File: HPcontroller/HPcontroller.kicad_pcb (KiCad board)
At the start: 2 copper layers, 100 x 62 mm, 45 parts, among them J1 Screw_Terminal_01x02, Q1 Q_Dual_NMOS_S1G1S2G2D2D2D1D1, U1 Adafruit_QTPY_ESP32-C3, U2 NCP81071B, U3 MIC841N, U4 VR10S3V3, U5 ER-OLED0.49-1_MODULE, U6 Adafruit_MAX31850

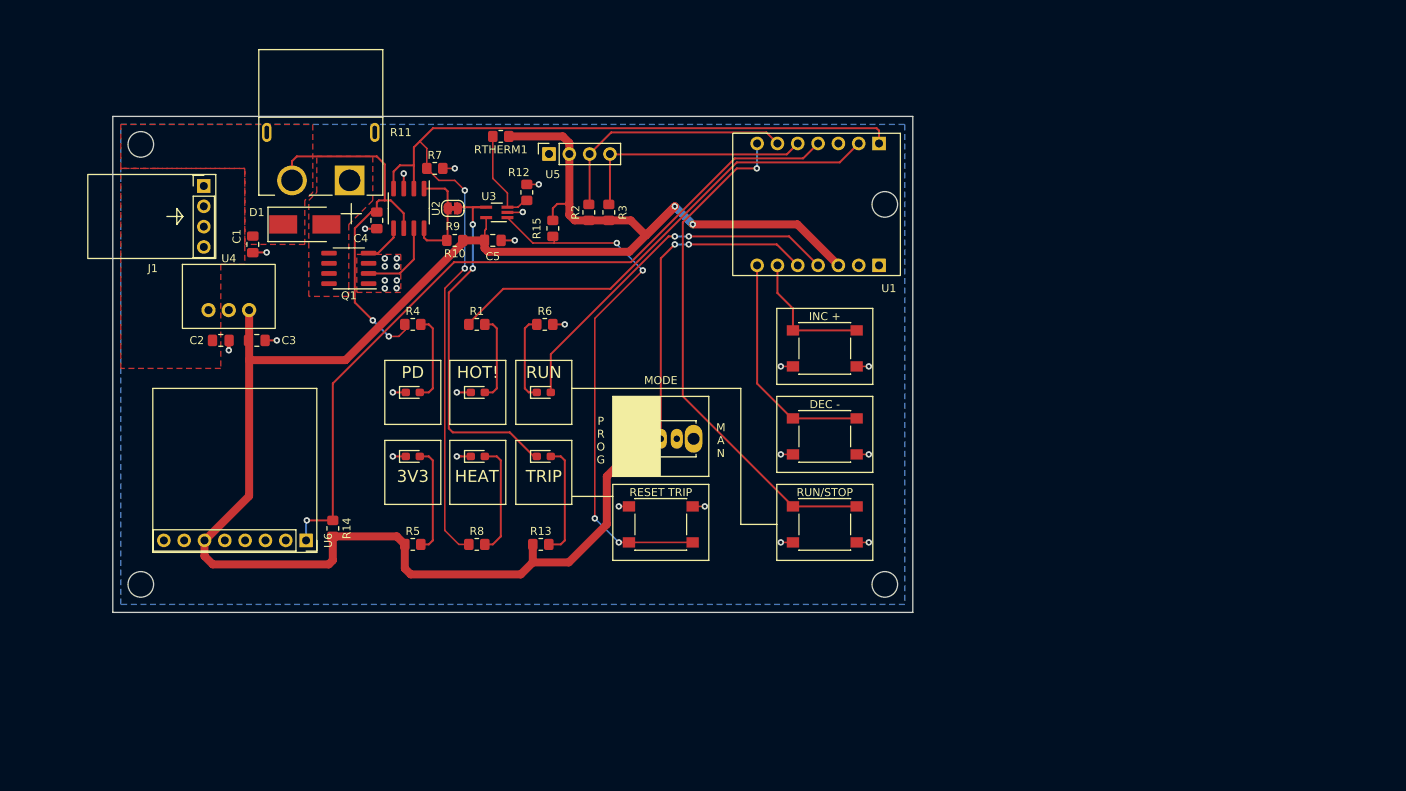
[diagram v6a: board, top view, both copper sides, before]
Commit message: started routing, finished footprintns
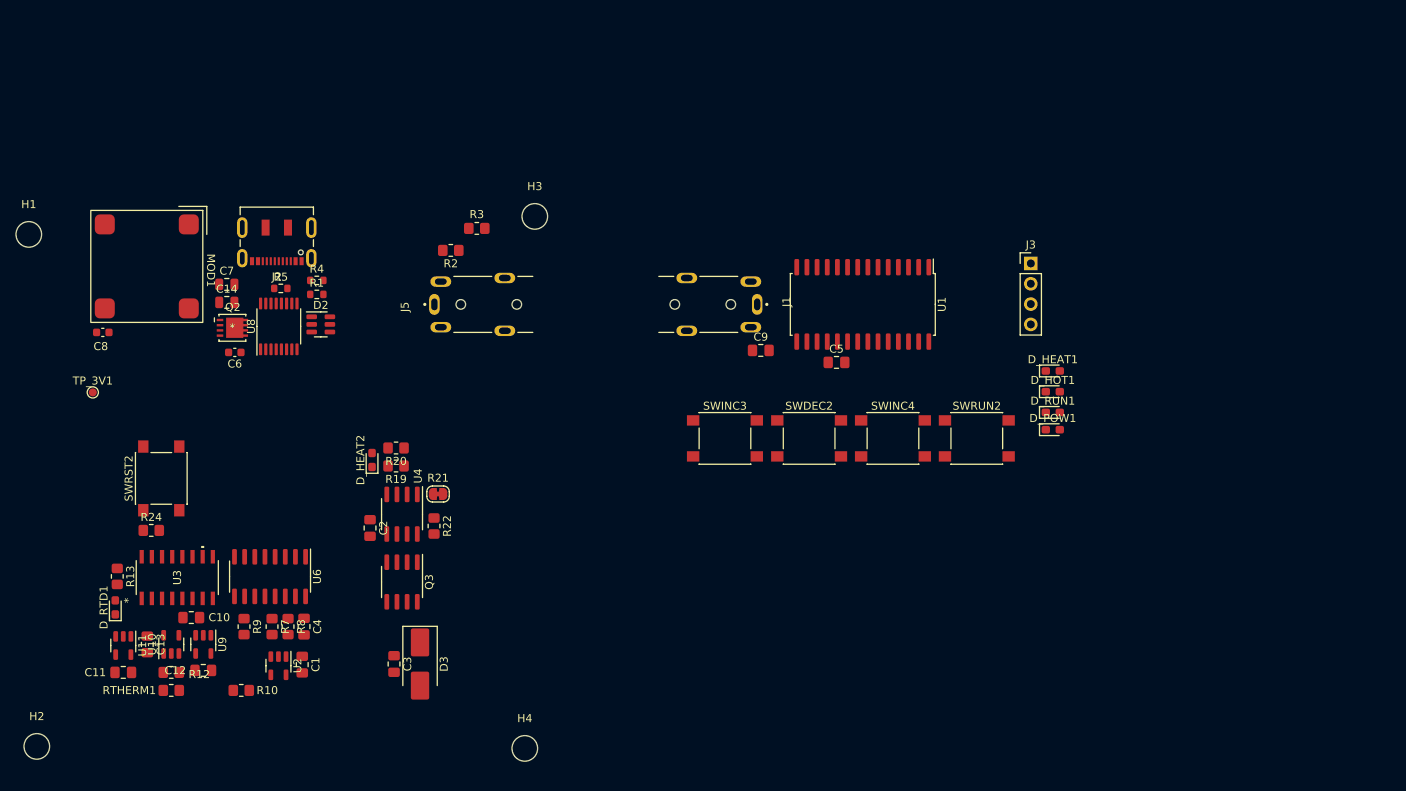
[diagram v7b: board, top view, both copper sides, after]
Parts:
- removed D1: D, Diode_SMD:D_SMB_Handsoldering
- removed D_3V3_POW1, D_PD_POW1: LED, LED_SMD:LED_0603_1608Metric_Pad1.05x0.95mm_HandSolder
- removed Q1: Q_Dual_NMOS_S1G1S2G2D2D2D1D1, Package_SO:SOIC-8_3.9x4.9mm_P1.27mm
- removed R11: R, connector_custom:AMASS_XT60PW-M
- removed R14: 4k7, Resistor_SMD:R_0805_2012Metric_Pad1.20x1.40mm_HandSolder
- removed R15: 10k, Resistor_SMD:R_0805_2012Metric_Pad1.20x1.40mm_HandSolder
- removed R6: 100, Resistor_SMD:R_0805_2012Metric_Pad1.20x1.40mm_HandSolder
- removed SWDEC1, SWINC1, SWRST1, SWRUN1: SW_SPST, Button_Switch_SMD:SW_SPST_PTS645
- removed SWMODE1: SW_SPDT, Button_Switch_THT:SW_Slide_1P2T_CK_OS102011MS2Q
- removed U5: ER-OLED0.49-1_MODULE, Connector_PinSocket_2.54mm:PinSocket_1x04_P2.54mm_Vertical
- added C10: 1uF, Capacitor_SMD:C_0805_2012Metric_Pad1.18x1.45mm_HandSolder, F.Cu at (82.8, 112.1)
- added C11: 1uF, Capacitor_SMD:C_0805_2012Metric_Pad1.18x1.45mm_HandSolder, F.Cu at (74.3, 119.0)
- added C12: 1uF, Capacitor_SMD:C_0805_2012Metric_Pad1.18x1.45mm_HandSolder, F.Cu at (84.3, 118.8)
- added C13: 1uF, Capacitor_SMD:C_0805_2012Metric_Pad1.18x1.45mm_HandSolder, F.Cu at (77.3, 115.5)
- added C14: 10uF, Capacitor_SMD:C_0805_2012Metric, F.Cu at (87.2, 72.8)
- added C6: 1uF, Capacitor_SMD:C_0603_1608Metric, F.Cu at (88.2, 79.0)
- added C7: 10uF, Capacitor_SMD:C_0805_2012Metric, F.Cu at (87.2, 70.5)
- added C8: 22uF, Capacitor_SMD:C_0603_1608Metric, F.Cu at (71.8, 76.5)
- added C9: 1uF, Capacitor_SMD:C_0805_2012Metric_Pad1.18x1.45mm_HandSolder, F.Cu at (154.0, 78.8)
- added D2: ESDA6V1BC6, Package_TO_SOT_SMD:SOT-23-6, F.Cu at (99.0, 75.5)
- added D3: D, Diode_SMD:D_SMB_Handsoldering, F.Cu at (111.4, 118.0)
- added D_HEAT2: LED, LED_SMD:LED_0603_1608Metric_Pad1.05x0.95mm_HandSolder, F.Cu at (105.4, 92.5)
- added D_POW1: LED, LED_SMD:LED_0603_1608Metric_Pad1.05x0.95mm_HandSolder, F.Cu at (190.5, 88.7)
- added J2: USB_C_Receptacle, Connector_USB:USB_C_Receptacle_JAE_DX07S016JA1R1500, F.Cu at (93.5, 64.5)
- added J3: Conn_01x04_Pin, Connector_PinHeader_2.54mm:PinHeader_1x04_P2.54mm_Vertical, F.Cu at (187.8, 67.9)
- added J5: 54-00174, HPfootprint:TENSILITY_54-00174, F.Cu at (120.0, 73.0)
- added MOD1: K7803JT-500R3-LB, HPfootprint:MORNSUN_K7803JT-500R3-LB, F.Cu at (77.2, 68.2)
- added Q2: AON7410, HPfootprint:DFN3X3A_8L_EPA1_P_AOS, F.Cu at (88.0, 75.9)
- added Q3: Q_Dual_NMOS_S1G1S2G2D2D2D1D1, Package_SO:SOIC-8_3.9x4.9mm_P1.27mm, F.Cu at (109.2, 107.7)
- added R19: 10k, Resistor_SMD:R_0805_2012Metric_Pad1.20x1.40mm_HandSolder, F.Cu at (108.4, 93.2)
- added R20: 100, Resistor_SMD:R_0805_2012Metric_Pad1.20x1.40mm_HandSolder, F.Cu at (108.4, 91.0)
- added R21: 0, Jumper:SolderJumper-2_P1.3mm_Bridged_RoundedPad1.0x1.5mm, F.Cu at (113.7, 96.7)
- added R22: 10k, Resistor_SMD:R_0805_2012Metric_Pad1.20x1.40mm_HandSolder, F.Cu at (113.2, 100.7)
- added R24: 10k, Resistor_SMD:R_0805_2012Metric_Pad1.20x1.40mm_HandSolder, F.Cu at (77.8, 101.2)
- added SWDEC2: SW_SPST, Button_Switch_SMD:SW_SPST_PTS645, F.Cu at (160.0, 89.8)
- added SWINC3: SW_SPST, Button_Switch_SMD:SW_SPST_PTS645, F.Cu at (149.5, 89.8)
- added SWINC4: SW_SPST, Button_Switch_SMD:SW_SPST_PTS645, F.Cu at (170.5, 89.8)
- added SWRST2: SW_SPST, Button_Switch_SMD:SW_SPST_PTS645, F.Cu at (79.1, 94.8)
- added SWRUN2: SW_SPST, Button_Switch_SMD:SW_SPST_PTS645, F.Cu at (181.0, 89.8)
- added TP_3V1: TestPoint, TestPoint:TestPoint_Pad_D1.0mm, F.Cu at (70.5, 84.0)
- added U10: SN74LVC1G14DBV, Package_TO_SOT_SMD:SOT-23-5, F.Cu at (80.3, 115.5)
- added U11: SN74LVC1G14DBV, Package_TO_SOT_SMD:SOT-23-5, F.Cu at (74.3, 115.6)
- added U8: IP2721, Package_SO:TSSOP-16_4.4x5mm_P0.65mm, F.Cu at (93.8, 75.8)
- added U9: SN74AHC1G08DBVR, Package_TO_SOT_SMD:SOT-23-5, F.Cu at (84.3, 115.5)
- C1: value 10u -> 1uF
- C2, C4, C5: value C -> 1uF
- C3: value C -> 10u
- J1: value Screw_Terminal_01x02 -> 54-00174; footprint connector_custom:PD_trigger -> HPfootprint:TENSILITY_54-00174
- R1: value 100 -> 5.1k; footprint Resistor_SMD:R_0805_2012Metric_Pad1.20x1.40mm_HandSolder -> Resistor_SMD:R_0603_1608Metric
- R10: value 10k -> RTHERM
- R4: value 1k5 -> 5.1k; footprint Resistor_SMD:R_0805_2012Metric_Pad1.20x1.40mm_HandSolder -> Resistor_SMD:R_0603_1608Metric
- R5: value 100 -> 100k; footprint Resistor_SMD:R_0805_2012Metric_Pad1.20x1.40mm_HandSolder -> Resistor_SMD:R_0603_1608Metric
- R7: value 10k -> 100k
- R8: value 100 -> 10k
- R9: value 0 -> 1k; footprint Jumper:SolderJumper-2_P1.3mm_Bridged_RoundedPad1.0x1.5mm -> Resistor_SMD:R_0805_2012Metric_Pad1.20x1.40mm_HandSolder
- U1: value Adafruit_QTPY_ESP32-C3 -> MCP23017_SO; footprint DevBoards:QTPY ESP32 C3 -> Package_SO:SOIC-28W_7.5x17.9mm_P1.27mm
- U2: value NCP81071B -> MCP3021A1T-E/OT; footprint Package_SO:SOIC-8_3.9x4.9mm_P1.27mm -> Package_TO_SOT_SMD:SOT-23-5
- U3: value MIC841N -> HEF4043BT; footprint Package_TO_SOT_SMD:SOT-353_SC-70-5_Handsoldering -> HPfootprint:SOT109-1_NXP
- U4: value VR10S3V3 -> NCP81071B; footprint DevBoards:3pinDCDC -> Package_SO:SOIC-8_3.9x4.9mm_P1.27mm
- U6: value Adafruit_MAX31850 -> SN74LV4052ADR; footprint Connector_PinSocket_2.54mm:PinSocket_1x08_P2.54mm_Vertical -> Package_SO:SOIC-16_3.9x9.9mm_P1.27mm
- moved H4 81.5 mm to (124.5, 128.5)
- moved RTHERM1 80.6 mm to (80.3, 121.2)
- moved H2 76.4 mm to (63.5, 128.2)
- moved R12 74.7 mm to (80.3, 119.0), turned to 0 degrees
- moved D_HEAT1 72.7 mm to (190.5, 81.3)
- moved D_HOT1 71.9 mm to (190.5, 83.9)
- moved D_RUN1 63.7 mm to (190.5, 86.5)
- moved H3 63.5 mm to (125.8, 62.0)
- moved J1 63.3 mm to (146.8, 73.0), turned to -90 degrees
- moved R10 62.3 mm to (89.1, 121.2), turned to 0 degrees
- moved R7 60.8 mm to (92.9, 113.3), turned to -90 degrees
- moved U3 60.7 mm to (81.1, 107.1), turned to 90 degrees
- moved U2 59.4 mm to (93.7, 118.2)
- moved R9 58.4 mm to (89.4, 113.3), turned to -90 degrees
- moved D_RTD1 56.8 mm to (73.3, 110.9), turned to 90 degrees
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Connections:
- C1 pad 1: VCC -> +3.3V
- C3 pad 1: +3V3 -> VCC
- C4 pad 1: VCC -> +3.3V
- D_HEAT1 pad 2: Net-(D_HEAT1-Pad2) -> /Controlpad/HEAT
- D_HOT1 pad 2: Net-(D_HOT1-Pad2) -> /Controlpad/HOT
- D_RTD1 pad 1: /ThermalProtector/THM_PROT_OUT -> /HEATER DRIVE/ENABLE_HEATER_DRIVE
- D_RUN1 pad 1: Net-(D_RUN1-Pad1) -> GND
- D_RUN1 pad 2: Net-(D_RUN1-Pad2) -> /Controlpad/RUN
- J1 pad 1: VCC -> GND
- J1 pad 2: GND -> /Controlpad/SDA
- R1 pad 1: Net-(R1-Pad1) -> /USB POWER IN/CC1
- R1 pad 2: Net-(D_HOT1-Pad2) -> GND
- R10 pad 1: +3V3 -> +3.3V
- R10 pad 2: Net-(R10-Pad2) -> Net-(U2-Ain)
- R12 pad 1: Net-(R12-Pad1) -> Net-(U3-1S)
- R4 pad 1: VCC -> /USB POWER IN/CC2
- R4 pad 2: Net-(D_PD_POW1-Pad2) -> GND
- R5 pad 1: +3V3 -> VBUS
- R7 pad 1: /FET_DRIVE -> Net-(U6-1Y1)
- R8 pad 1: /FET_DRIVE -> Net-(U6-1Y2)
- R8 pad 2: Net-(D_HEAT1-Pad2) -> GND
- R9 pad 1: /ThermalProtector/THM_PROT_OUT -> Net-(U6-1Y3)
- R9 pad 2: Net-(R10-Pad2) -> GND
- RTHERM1 pad 2: Net-(R12-Pad1) -> Net-(U3-1S)
- U1 pad 1: /FET_DRIVE -> /Controlpad/HEAT
- U1 pad 10: /MODE -> GND
- U1 pad 11: Net-(D_RUN1-Pad2) -> unconnected-(U1-NC-Pad11)
- U1 pad 12: +3V3 -> /Controlpad/SCL
- U1 pad 13: GND -> /Controlpad/SDA
- U1 pad 2: Net-(R1-Pad1) -> /Controlpad/RUN
- U1 pad 3: unconnected-(U1-Pad3) -> /Controlpad/HOT
- U1 pad 4: /OW_DATA -> /Controlpad/POW
- U1 pad 5: /SDA -> unconnected-(U1-GPB4-Pad5)
- U1 pad 6: /SCL -> unconnected-(U1-GPB5-Pad6)
- U1 pad 7: /RUN -> unconnected-(U1-GPB6-Pad7)
- U1 pad 8: /DEC -> unconnected-(U1-GPB7-Pad8)
- U1 pad 9: /INC -> +3V3
- U2 pad 1: Net-(R10-Pad2) -> +3.3V
- U2 pad 2: /FET_DRIVE -> GND
- U2 pad 3: GND -> Net-(U2-Ain)
- U2 pad 4: /FET_DRIVE -> /SDA
- U2 pad 5: /OUTB -> /SCL
- U3 pad 1: /ThermalProtector/THM_PROT_RES -> unconnected-(U3-4Q-Pad1)
- U3 pad 2: GND -> /ThermalProtector/QOUT
- U3 pad 3: Net-(R12-Pad1) -> Net-(U3-1R)
- U3 pad 4: /ThermalProtector/THM_PROT_OUT -> Net-(U3-1S)
- U4 pad 1: VCC -> Net-(U4-ENA)
- U4 pad 2: GND -> /HEAT_DRIVE
- U4 pad 3: +3V3 -> GND
- U6 pad 1: /OW_DATA -> unconnected-(U6-2Y0-Pad1)
- U6 pad 6: +3V3 -> GND
- U6 pad 7: unconnected-(U6-Pad7) -> GND
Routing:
- net +3V3: track 235.5 -> 0.00 mm, vias 2 -> 0
- net /FET_DRIVE: track 127.9 -> 0.00 mm, vias 2 -> 0
- net /OW_DATA: track 96.0 -> 0.00 mm, vias 1 -> 0
- net /ThermalProtector/THM_PROT_RES: track 67.6 -> 0.00 mm, vias 4 -> 0
- net /RUN: track 64.3 -> 0.00 mm, vias 1 -> 0
- net Net-(R1-Pad1): track 58.2 -> 0.00 mm
- net VCC: track 48.3 -> 0.00 mm, vias 2 -> 0
- net /ThermalProtector/THM_PROT_OUT: track 46.6 -> 0.00 mm, vias 2 -> 0
- net Net-(D_RUN1-Pad2): track 45.8 -> 0.00 mm, vias 2 -> 0
- net /MODE: track 41.5 -> 0.00 mm, vias 2 -> 0
- net GND: track 34.6 -> 0.00 mm, vias 30 -> 0
- net /SCL: track 31.5 -> 0.00 mm
- net /SDA: track 30.4 -> 0.00 mm
- net /DEC: track 29.5 -> 0.00 mm
- net /INC: track 16.9 -> 0.00 mm
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- removed copper zone on B.Cu, net GND
- removed copper zone on F.Cu, net GND
- removed copper zone on F.Cu, net Net-(D1-Pad2)
- removed copper zone on F.Cu, net VCC
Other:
- board outline removed
- board text removed: "3V3"
- board text removed: "DEC -"
- board text removed: "HEAT"
- board text removed: "HOT!"
- board text removed: "INC +"
- board text removed: "M A N"
- board text removed: "MODE"
- board text removed: "P R O G"
- board text removed: "PD"
- board text removed: "RESET TRIP"
- board text removed: "RUN"
- board text removed: "RUN/STOP"
- board text removed: "TRIP"

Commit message: finished routing, moving on to heater
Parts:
- removed H1, H4: MountingHole, MountingHole:MountingHole_3.2mm_M3_ISO14580
- removed TP_3V1: TestPoint, TestPoint:TestPoint_Pad_D1.0mm
- added J4: Conn_01x01_Pin, HPfootprint:S7051-42R, F.Cu at (168.6, 101.2)
- added J6: Conn_01x01_Pin, HPfootprint:S7051-42R, F.Cu at (174.1, 101.2)
- added U7: Adafruit_QTPY_ESP32-C3, HPfootprint:QTPY ESP32 C3, F.Cu at (132.4, 79.2)
- H2, H3: footprint MountingHole:MountingHole_3.2mm_M3_ISO14580 -> MountingHole:MountingHole_2.7mm_M2.5
- R21: moved to B.Cu
- moved C6 75.0 mm to (161.4, 95.8)
- moved MOD1 74.9 mm to (148.9, 90.2)
- moved C7 72.4 mm to (158.1, 85.2)
- moved C14 72.3 mm to (158.1, 87.2)
- moved R5 72.3 mm to (164.9, 85.2), turned to -90 degrees
- moved SWRST2 72.2 mm to (149.4, 78.2), turned to 180 degrees
- moved Q2 72.1 mm to (158.4, 91.2)
- moved H2 72.0 mm to (134.4, 115.8)
- moved U8 71.7 mm to (163.9, 90.8)
- moved C8 70.8 mm to (139.6, 96.8), turned to 180 degrees
- moved D2 70.7 mm to (168.9, 86.2), turned to 90 degrees
- moved J2 69.8 mm to (161.9, 78.8)
- moved R24 68.5 mm to (142.9, 79.8), turned to 90 degrees
- moved Q3 66.8 mm to (173.4, 89.2)
- moved U4 66.8 mm to (172.9, 79.3)
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- renumbered RTHERM1 to RTHERM
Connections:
- C1 pad 1: +3.3V -> +3V3
- C2 pad 1: VCC -> +20V_USBPD
- C3 pad 1: VCC -> +20V_USBPD
- C4 pad 1: +3.3V -> +3V3
- C8 pad 1: +3.3V -> +3V3
- D2 pad 1: /USB POWER IN/CC1 -> /USB POWER IN/CC2
- D2 pad 3: /USB POWER IN/CC2 -> /USB POWER IN/CC1
- D3 pad 1: VCC -> +20V_USBPD
- D_RUN1 pad 2: /Controlpad/RUN -> /Controlpad/RUN_LED
- J1 pad 2: /Controlpad/SDA -> /SDA
- J1 pad 4_1: /Controlpad/SCL -> /SCL
- J1 pad 4_2: /Controlpad/SCL -> /SCL
- J3 pad 3: /Controlpad/SCL -> /SCL
- J3 pad 4: /Controlpad/SDA -> /SDA
- MOD1 pad 3: +3.3V -> +3V3
- R10 pad 1: +3.3V -> +3V3
- U1 pad 12: /Controlpad/SCL -> /SCL
- U1 pad 13: /Controlpad/SDA -> /SDA
- U1 pad 2: /Controlpad/RUN -> /Controlpad/RUN_LED
- U1 pad 20: /Controlpad/INTA -> /INTA
- U1 pad 22: /Controlpad/INC -> /Controlpad/DEC
- U1 pad 23: /Controlpad/DEC -> /Controlpad/INC
- U2 pad 1: +3.3V -> +3V3
- U4 pad 6: VCC -> +20V_USBPD
- U6 pad 16: +3.3V -> +3V3
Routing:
- net /SDA: track 0.00 -> 139.2 mm, vias 0 -> 2
- net /SCL: track 0.00 -> 128.0 mm, vias 0 -> 3
- net GND: track 0.00 -> 122.5 mm, vias 0 -> 43
- net /INTA: track 0.00 -> 91.0 mm, vias 0 -> 2
- net /HEATER DRIVE/ENABLE_HEATER_DRIVE: track 0.00 -> 74.8 mm, vias 0 -> 2
- net /HEAT_DRIVE: track 0.00 -> 57.2 mm
- net +20V_USBPD: track 0.00 -> 55.2 mm, vias 0 -> 2
- net +3V3: track 0.00 -> 54.3 mm, vias 0 -> 16
- net Net-(SWRST2-A): track 0.00 -> 48.0 mm, vias 0 -> 2
- net Net-(U3-1S): track 0.00 -> 42.2 mm
- net Net-(U2-Ain): track 0.00 -> 41.5 mm
- net Net-(U4-ENA): track 0.00 -> 39.6 mm, vias 0 -> 2
- net /Controlpad/RUN_LED: track 0.00 -> 29.3 mm
- net /Controlpad/HOT: track 0.00 -> 28.4 mm
- net /Controlpad/POW: track 0.00 -> 28.1 mm
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- added copper zone on F.Cu, net +20V_USBPD
- added copper zone on In2.Cu, net +3V3
- added copper zone on In1.Cu, net GND
- added copper zone on F.Cu, net Net-(D3-A)
- added copper zone on F.Cu, net VBUS
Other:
- board outline added: 78 x 57 mm
- copper layers 2 -> 4
- board text added: "HP_POWER"
